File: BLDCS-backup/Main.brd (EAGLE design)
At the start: 27.9 x 73.7 mm, 60 parts, among them IC1 MEGA8-AI, IC3 TP4056, J1 PIC_ICSP_MINI_5_PIN, U4 LM1117 3.3, X1 MINI-USB-32005-201, Y1 16MHZ

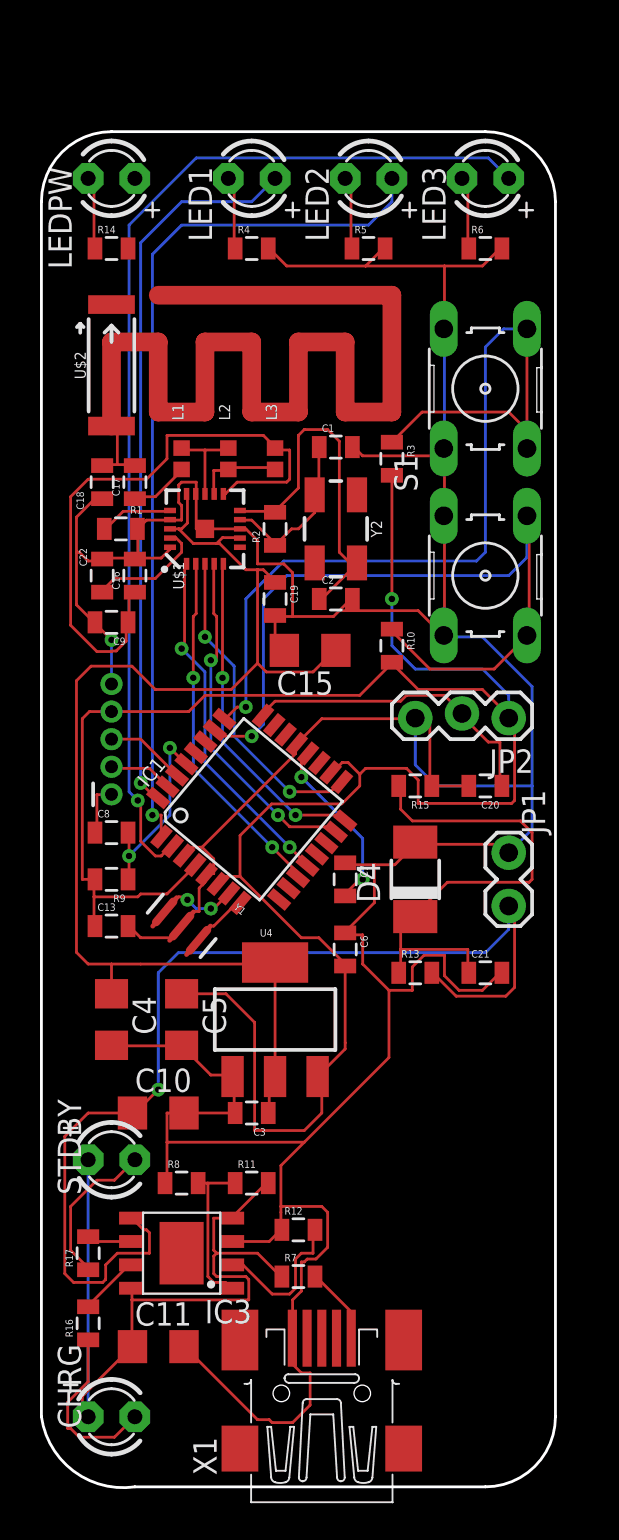
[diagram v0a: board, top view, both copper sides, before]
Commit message: add license
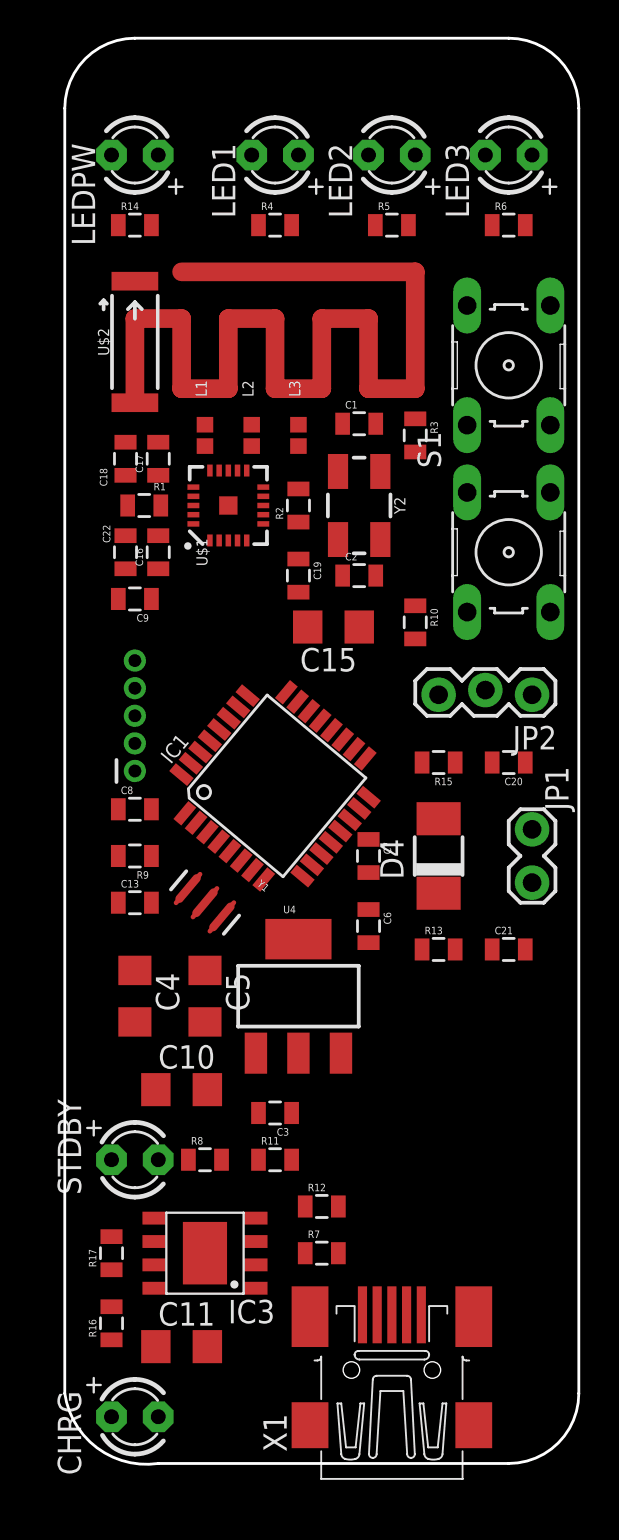
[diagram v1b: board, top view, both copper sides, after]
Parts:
- moved X1 4.02 mm to (17.8, 5.08)
- moved LEDPW 1.80 mm to (3.81, 71.1)
- moved LED1 1.80 mm to (11.4, 71.1)
- moved LED2 1.80 mm to (17.8, 71.1)
- moved LED3 1.80 mm to (24.1, 71.1)
- moved C7 1.80 mm to (16.5, 33.0)
- moved L1 1.80 mm to (7.62, 55.9)
- moved U$1 1.80 mm to (8.89, 52.1)
- moved C16 1.80 mm to (5.08, 49.5)
- moved C22 1.80 mm to (3.30, 49.5)
- moved C8 1.80 mm to (3.81, 35.6)
- moved C9 1.80 mm to (3.81, 47.0)
- moved J1 1.80 mm to (3.81, 40.6)
- moved R9 1.80 mm to (3.81, 33.0)
- moved U$2 1.80 mm to (3.81, 61.0)
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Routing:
- net GND: track 242.0 -> 0.00 mm, vias 1 -> 0
- net VCC: track 122.1 -> 0.00 mm, vias 1 -> 0
- net 3.3V: track 67.9 -> 0.00 mm
- net BATT_IN: track 59.6 -> 0.00 mm, vias 1 -> 0
- net D4: track 58.7 -> 0.00 mm, vias 1 -> 0
- net A2: track 51.3 -> 0.00 mm, vias 1 -> 0
- net D3: track 47.6 -> 0.00 mm, vias 1 -> 0
- net A3: track 43.1 -> 0.00 mm, vias 1 -> 0
- net N$25: track 43.0 -> 0.00 mm
- net D2: track 39.4 -> 0.00 mm, vias 1 -> 0
- net N$16: track 33.9 -> 0.00 mm
- net A0: track 27.8 -> 0.00 mm
- net D7: track 19.5 -> 0.00 mm, vias 2 -> 0
- net D8: track 19.5 -> 0.00 mm, vias 2 -> 0
- net N$21: track 19.4 -> 0.00 mm
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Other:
- board size 27.9 x 73.7 mm -> 27.9 x 77.5 mm
